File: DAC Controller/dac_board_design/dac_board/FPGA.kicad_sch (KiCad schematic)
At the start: 0 parts

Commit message: Add Decoupling
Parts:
- added C10, C11, C15, C16, C17, C18, C6: .47µf, symbol Device:C
- added C12, C5: 47µf, symbol Device:C
- added C13, C14, C8, C9: 4.7µf, symbol Device:C
- added C7: 100µf, symbol Device:C
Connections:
- new net +1V0: C10.1, C10.2, C11.1, C11.2, C12.1, C12.2, C13.1, C13.2, C14.1, C14.2, C15.1, C15.2, C16.1, C16.2, C17.1, C17.2, C18.1, C18.2, C5.1, C5.2, C6.1, C6.2, C7.1, C7.2, C8.1, C8.2, C9.1, C9.2

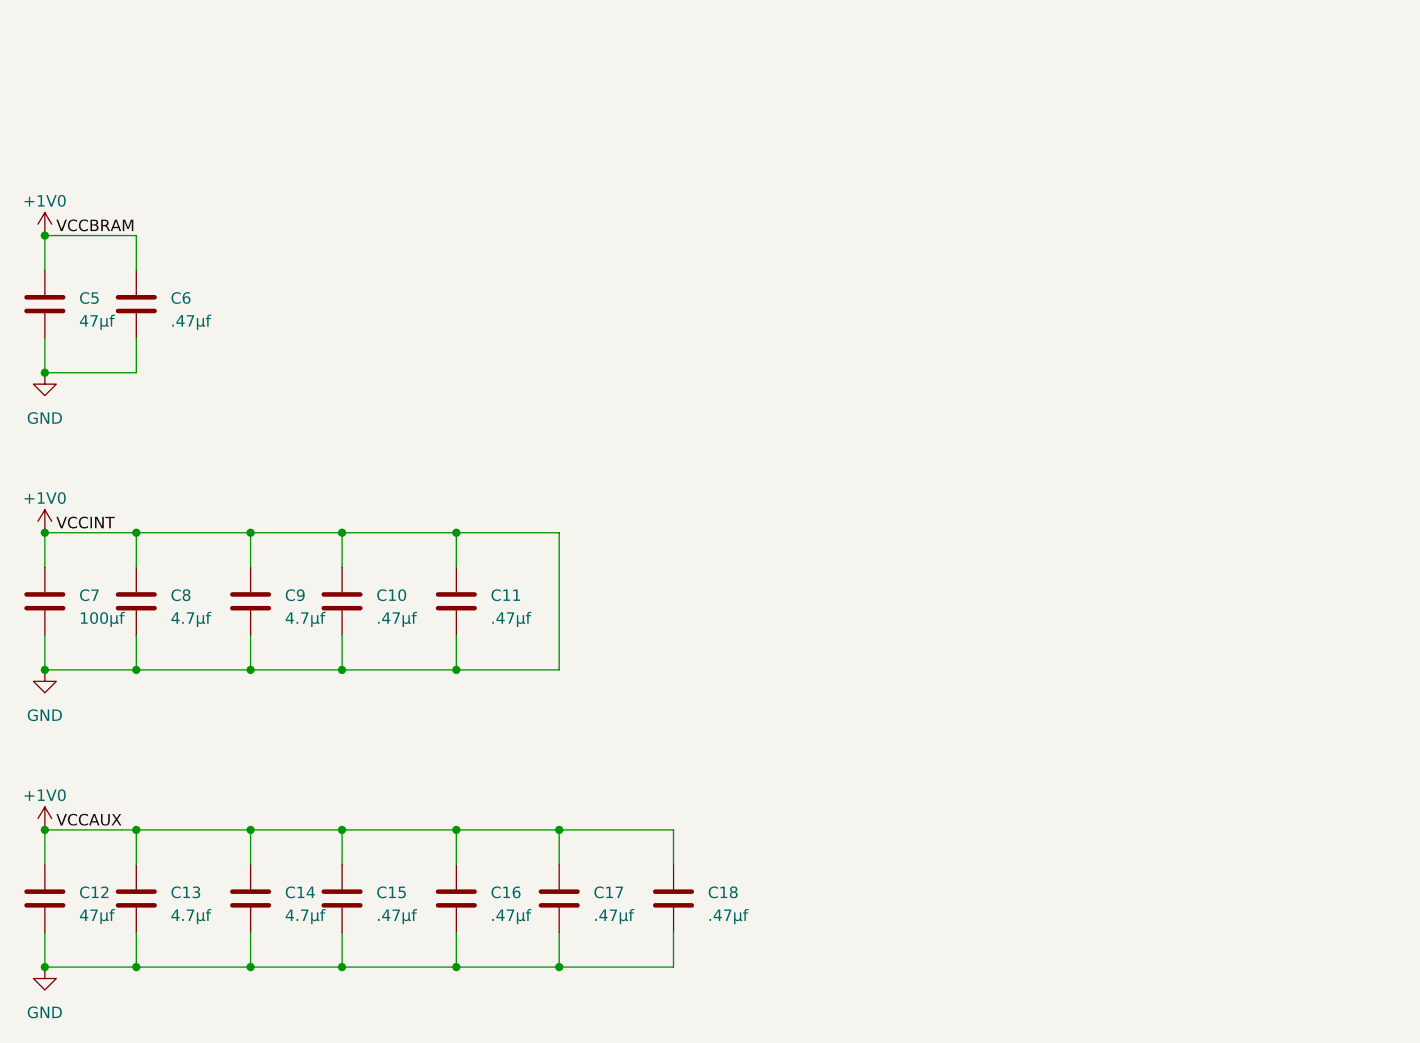
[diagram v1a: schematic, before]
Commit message: Add Fpga Power Pins
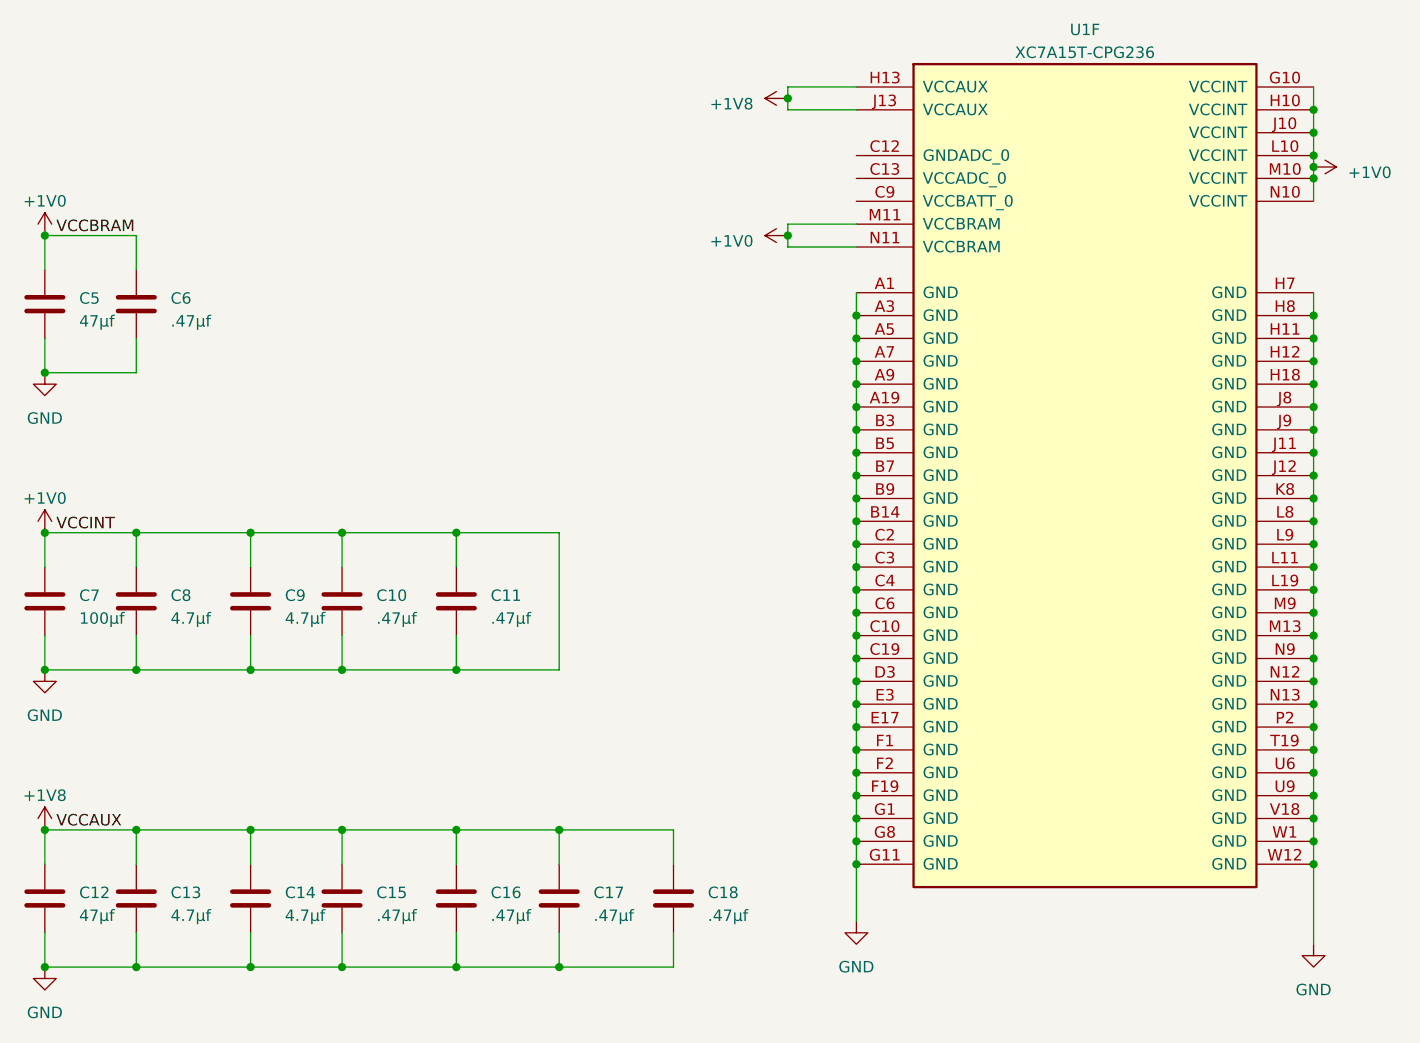
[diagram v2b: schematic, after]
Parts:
- added U1: XC7A15T-CPG236, symbol FPGA_Xilinx_Artix7:XC7A15T-CPG236
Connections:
- net +1V0: now also U1.A1 (GND), U1.A19 (GND), U1.A3 (GND), U1.A5 (GND), U1.A7 (GND), U1.A9 (GND), U1.B14 (GND), U1.B3 (GND), U1.B5 (GND), U1.B7 (GND), U1.B9 (GND), U1.C10 (GND), U1.C19 (GND), U1.C2 (GND), U1.C3 (GND), U1.C4 (GND), U1.C6 (GND), U1.D3 (GND), U1.E17 (GND), U1.E3 (GND), U1.F1 (GND), U1.F19 (GND), U1.F2 (GND), U1.G1 (GND), U1.G10 (VCCINT), U1.G11 (GND), U1.G8 (GND), U1.H10 (VCCINT), U1.H11 (GND), U1.H12 (GND), U1.H18 (GND), U1.H7 (GND), U1.H8 (GND), U1.J10 (VCCINT), U1.J11 (GND), U1.J12 (GND), U1.J8 (GND), U1.J9 (GND), U1.K8 (GND), U1.L10 (VCCINT), U1.L11 (GND), U1.L19 (GND), U1.L8 (GND), U1.L9 (GND), U1.M10 (VCCINT), U1.M11 (VCCBRAM), U1.M13 (GND), U1.M9 (GND), U1.N10 (VCCINT), U1.N11 (VCCBRAM), U1.N12 (GND), U1.N13 (GND), U1.N9 (GND), U1.P2 (GND), U1.T19 (GND), U1.U6 (GND), U1.U9 (GND), U1.V18 (GND), U1.W1 (GND), U1.W12 (GND); no longer C12.1, C13.1, C14.1, C15.1, C16.1, C17.1, C18.1
- new net +1V8: C12.1, C13.1, C14.1, C15.1, C16.1, C17.1, C18.1, U1.H13 (VCCAUX), U1.J13 (VCCAUX)
